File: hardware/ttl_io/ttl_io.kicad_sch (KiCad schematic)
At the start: 26 parts, among them J13 Conn_02x08_Counter_Clockwise, J14 Conn_02x08_Counter_Clockwise, SW3 SW_SPDT, U14 74CBTLV3245, U16 74CBTLV3245, U17 74CBTLV3245, U19 TXB0108

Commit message: update pcb and bom
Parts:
- J13, J14: Link (none) -> https://www.digikey.com/en/products/detail/w%C3%BCrth-elekt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; Manufacturer (none) -> Würth Elektronik; Manufacturer Number (none) -> 610116249121
- SW3: Notes 6V max -> 6V max, may not be washable.
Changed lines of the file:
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@@
       (effects (font (size 1.27 1.27)) hide)
     )
-    (property "Datasheet" "~" (at 86.36 40.005 0)
+    (property "Datasheet" "https://www.we-online.com/components/products/datasheet/6101xx249121.pdf" (at 86.36 40.005 0)
+      (effects (font (size 1.27 1.27)) hide)
+    )
+    (property "Link" "https://www.digikey.com/en/products/detail/w%C3%BCrth-elektronik/610116249121/5047737" (at 86.36 40.005 0)
+      (effects (font (size 1.27 1.27)) hide)
+    )
+    (property "Manufacturer" "Würth Elektronik" (at 86.36 40.005 0)
+      (effects (font (size 1.27 1.27)) hide)
+    )
+    (property "Manufacturer Number" "610116249121" (at 86.36 40.005 0)
       (effects (font (size 1.27 1.27)) hide)
     )
@@
   (symbol (lib_id "Logic_LevelTranslator:TXB0108DQSR") (at 119.38 42.545 180) (unit 1)
     (in_bom yes) (on_board yes) (dnp no)
-    (property "Reference" "U19" (at 125.095 25.4 0)
-      (effects (font (size 1.27 1.27)) (justify left))
-    )
-    (property "Value" "TXB0108" (at 134.62 22.86 0)
-      (effects (font (size 1.27 1.27)) (justify left))
+    (property "Reference" "U19" (at 121.92 23.495 0)
+      (effects (font (size 1.27 1.27)) (justify right))
+    )
+    (property "Value" "TXB0108" (at 121.92 26.035 0)
+      (effects (font (size 1.27 1.27)) (justify right))
     )
     (property "Footprint" "Package_SO:TSSOP-20_4.4x6.5mm_P0.65mm" (at 119.38 23.495 0)
@@
       (effects (font (size 1.27 1.27)) hide)
     )
-    (property "Notes" "6V max" (at 87.63 61.595 90)
+    (property "Notes" "6V max, may not be washable." (at 87.63 61.595 90)
       (effects (font (size 1.27 1.27)) hide)
     )
@@
       (effects (font (size 1.27 1.27)) hide)
     )
-    (property "Datasheet" "~" (at 90.805 166.37 0)
-      (effects (font (size 1.27 1.27)) hide)
-    )
+    (property "Datasheet" "https://www.we-online.com/components/products/datasheet/6101xx249121.pdf" (at 90.805 166.37 0)
+      (effects (font (size 1.27 1.27)) hide)
+    )
+    (property "Link" "https://www.digikey.com/en/products/detail/w%C3%BCrth-elektronik/610116249121/5047737" (at 90.805 166.37 0)
+      (effects (font (size 1.27 1.27)) hide)
+    )
+    (property "Manufacturer" "Würth Elektronik" (at 90.805 166.37 0)
+      (effects (font (size 1.27 1.27)) hide)
+    )
+    (property "Manufacturer Number" "610116249121" (at 90.805 166.37 0)
+      (effects (font (size 1.27 1.27)) hide)
+    )

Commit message: draft scheduler
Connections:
- net EXT_DIR0: now also J13.9 (Pin_9); no longer J13.16 (Pin_16)
- net EXT_DIR1: now also J13.10 (Pin_10); no longer J13.15 (Pin_15)
- net EXT_DIR2: now also J13.11 (Pin_11); no longer J13.14 (Pin_14)
- net EXT_DIR3: now also J13.12 (Pin_12); no longer J13.13 (Pin_13)
- net EXT_DIR4: now also J13.13 (Pin_13); no longer J13.12 (Pin_12)
- net EXT_DIR5: now also J13.14 (Pin_14); no longer J13.11 (Pin_11)
- net EXT_DIR6: now also J13.15 (Pin_15); no longer J13.10 (Pin_10)
- net EXT_DIR7: now also J13.16 (Pin_16); no longer J13.9 (Pin_9)
- net EXT_IN0: now also J14.9 (Pin_9); no longer J14.16 (Pin_16)
- net EXT_IN1: now also J14.10 (Pin_10); no longer J14.15 (Pin_15)
- net EXT_IN2: now also J14.11 (Pin_11); no longer J14.14 (Pin_14)
- net EXT_IN3: now also J14.12 (Pin_12); no longer J14.13 (Pin_13)
- net EXT_IN4: now also J14.13 (Pin_13); no longer J14.12 (Pin_12)
- net EXT_IN5: now also J14.14 (Pin_14); no longer J14.11 (Pin_11)
- net EXT_IN6: now also J14.15 (Pin_15); no longer J14.10 (Pin_10)
- net EXT_IN7: now also J14.16 (Pin_16); no longer J14.9 (Pin_9)
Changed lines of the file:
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@@
     )
   )
-  (symbol (lib_id "Connector_Generic:Conn_02x08_Counter_Clockwise") (at 86.36 40.005 0) (unit 1)
+  (symbol (lib_id "Connector_Generic:Conn_02x08_Counter_Clockwise") (at 86.36 42.545 0) (mirror x) (unit 1)
     (in_bom yes) (on_board yes) (dnp no)
     (property "Reference" "J14" (at 87.63 29.845 0)
       (effects (font (size 1.27 1.27)))
     )
-    (property "Value" "Conn_02x08_Counter_Clockwise" (at 87.63 28.575 0)
-      (effects (font (size 1.27 1.27)) hide)
-    )
-    (property "Footprint" "kicad_component_library:PinHeader_2x08_P2.54mm_Horizontal_SMD" (at 86.36 40.005 0)
-      (effects (font (size 1.27 1.27)) hide)
-    )
-    (property "Datasheet" "https://www.we-online.com/components/products/datasheet/6101xx249121.pdf" (at 86.36 40.005 0)
-      (effects (font (size 1.27 1.27)) hide)
-    )
-    (property "Link" "https://www.digikey.com/en/products/detail/w%C3%BCrth-elektronik/610116249121/5047737" (at 86.36 40.005 0)
-      (effects (font (size 1.27 1.27)) hide)
-    )
-    (property "Manufacturer" "Würth Elektronik" (at 86.36 40.005 0)
-      (effects (font (size 1.27 1.27)) hide)
-    )
-    (property "Manufacturer Number" "610116249121" (at 86.36 40.005 0)
+    (property "Value" "Conn_02x08_Counter_Clockwise" (at 87.63 53.975 0)
+      (effects (font (size 1.27 1.27)) hide)
+    )
+    (property "Footprint" "kicad_component_library:PinHeader_2x08_P2.54mm_Horizontal_SMD" (at 86.36 42.545 0)
+      (effects (font (size 1.27 1.27)) hide)
+    )
+    (property "Datasheet" "https://www.we-online.com/components/products/datasheet/610116249121.pdf" (at 86.36 42.545 0)
+      (effects (font (size 1.27 1.27)) hide)
+    )
+    (property "Link" "https://www.digikey.com/en/products/detail/w%C3%BCrth-elektronik/610116249121/5047737" (at 86.36 42.545 0)
+      (effects (font (size 1.27 1.27)) hide)
+    )
+    (property "Manufacturer" "Würth Elektronik" (at 86.36 42.545 0)
+      (effects (font (size 1.27 1.27)) hide)
+    )
+    (property "Manufacturer Number" "610116249121" (at 86.36 42.545 0)
       (effects (font (size 1.27 1.27)) hide)
     )
@@
     )
   )
-  (symbol (lib_id "Connector_Generic:Conn_02x08_Counter_Clockwise") (at 90.805 166.37 0) (unit 1)
+  (symbol (lib_id "Connector_Generic:Conn_02x08_Counter_Clockwise") (at 90.805 168.91 0) (mirror x) (unit 1)
     (in_bom yes) (on_board yes) (dnp no)
     (property "Reference" "J13" (at 92.075 156.21 0)
       (effects (font (size 1.27 1.27)))
     )
-    (property "Value" "Conn_02x08_Counter_Clockwise" (at 92.075 154.94 0)
-      (effects (font (size 1.27 1.27)) hide)
-    )
-    (property "Footprint" "kicad_component_library:PinHeader_2x08_P2.54mm_Horizontal_SMD" (at 90.805 166.37 0)
-      (effects (font (size 1.27 1.27)) hide)
-    )
-    (property "Datasheet" "https://www.we-online.com/components/products/datasheet/6101xx249121.pdf" (at 90.805 166.37 0)
-      (effects (font (size 1.27 1.27)) hide)
-    )
-    (property "Link" "https://www.digikey.com/en/products/detail/w%C3%BCrth-elektronik/610116249121/5047737" (at 90.805 166.37 0)
-      (effects (font (size 1.27 1.27)) hide)
-    )
-    (property "Manufacturer" "Würth Elektronik" (at 90.805 166.37 0)
-      (effects (font (size 1.27 1.27)) hide)
-    )
-    (property "Manufacturer Number" "610116249121" (at 90.805 166.37 0)
-      (effects (font (size 1.27 1.27)) hide)
-    )
+    (property "Value" "Conn_02x08_Counter_Clockwise" (at 92.075 180.34 0)
+      (effects (font (size 1.27 1.27)) hide)
+    )
+    (property "Footprint" "kicad_component_library:PinHeader_2x08_P2.54mm_Horizontal_SMD" (at 90.805 168.91 0)
+      (effects (font (size 1.27 1.27)) hide)
+    )
+    (property "Datasheet" "https://www.we-online.com/components/products/datasheet/610116249121.pdf" (at 90.805 168.91 0)
+      (effects (font (size 1.27 1.27)) hide)
+    )
+    (property "Link" "https://www.digikey.com/en/products/detail/w%C3%BCrth-elektronik/610116249121/5047737" (at 90.805 168.91 0)
+      (effects (font (size 1.27 1.27)) hide)
+    )
+    (property "Manufacturer" "Würth Elektronik" (at 90.805 168.91 0)
+      (effects (font (size 1.27 1.27)) hide)
+    )
+    (property "Manufacturer Number" "610116249121" (at 90.805 168.91 0)
+      (effects (font (size 1.27 1.27)) hide)
+    )

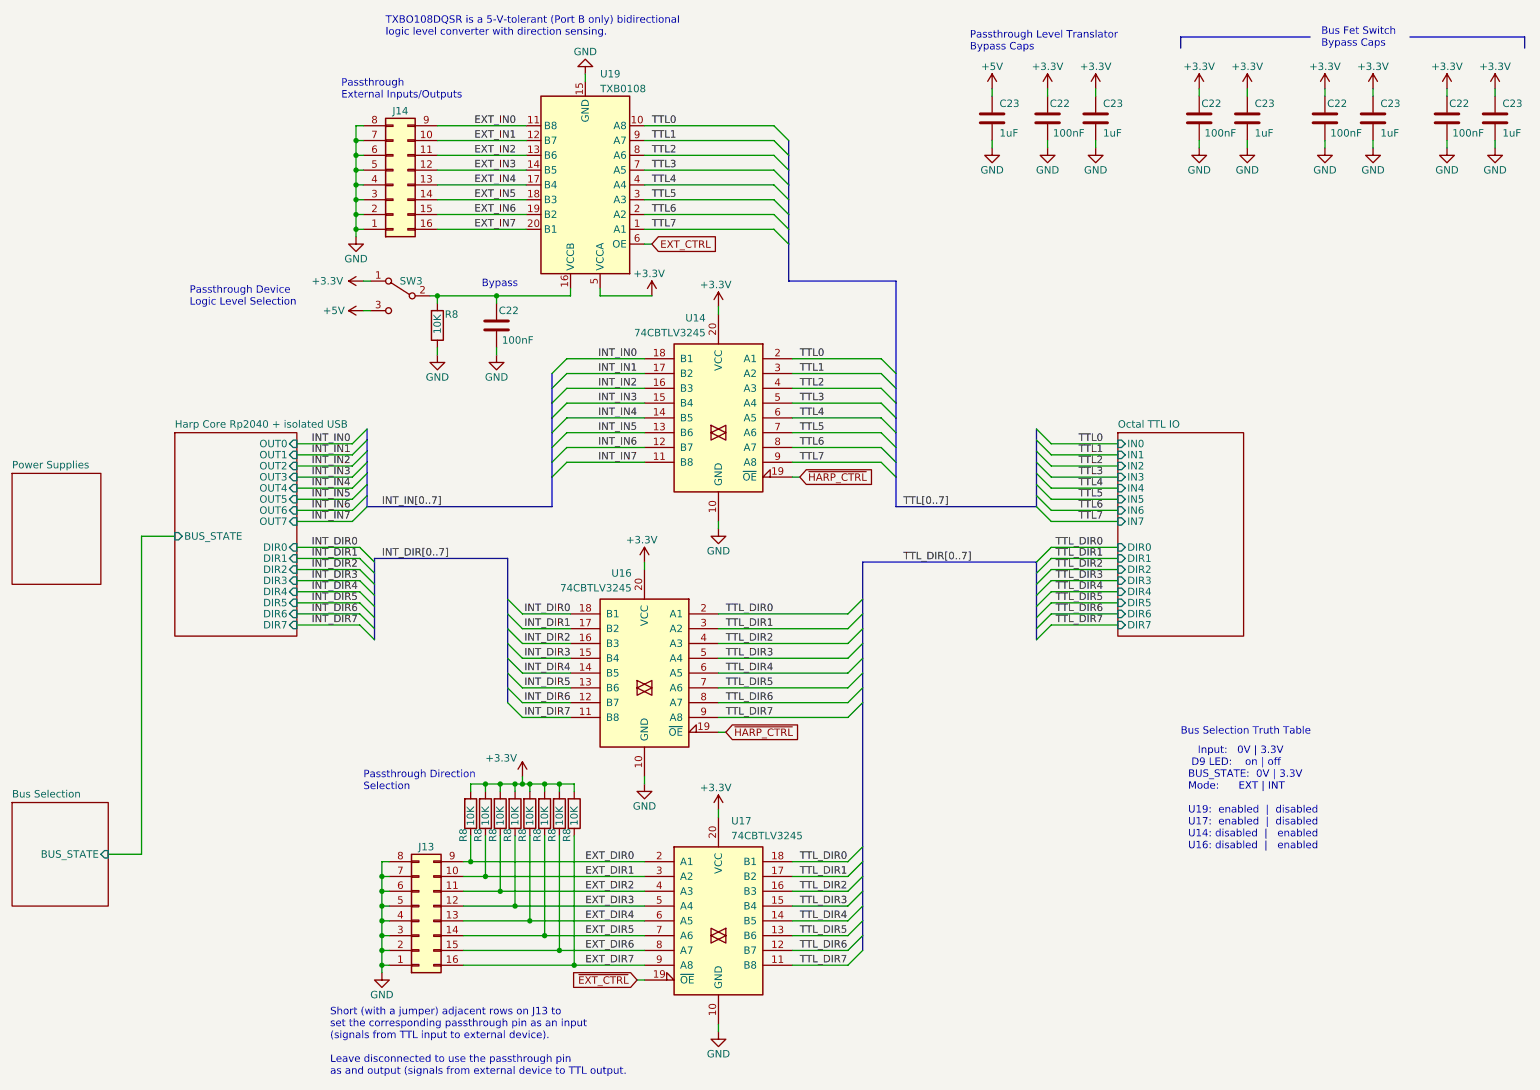
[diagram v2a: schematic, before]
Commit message: get pwm task and ios working
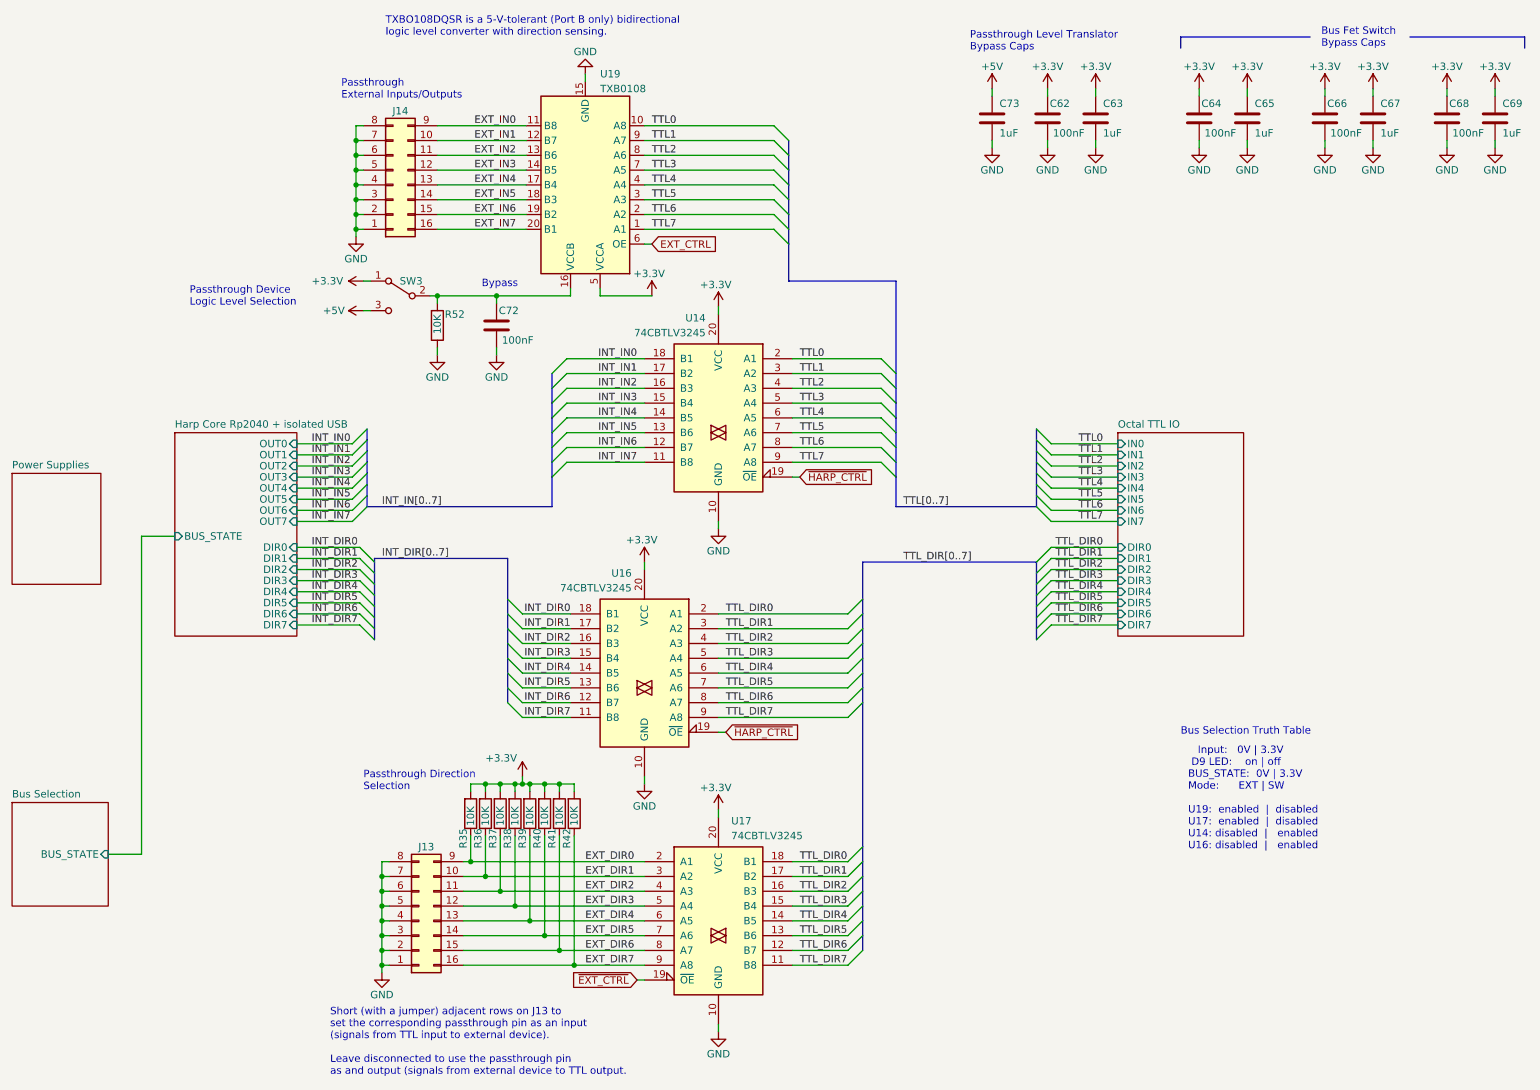
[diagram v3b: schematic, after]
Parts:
- renumbered C22 to C62, C23 to C63, C22 to C64, C23 to C65, C22 to C66, C23 to C67, C22 to C68, C23 to C69, C22 to C72, C23 to C73, R8 to R35, R8 to R36, R8 to R37, R8 to R38, R8 to R39, R8 to R40, R8 to R41, R8 to R42, R8 to R52
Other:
- note added: "Input: 0V | 3.3V D9 LED: on | off BUS_STATE: 0V | 3.3V Mode: EXT | SW U19: enabled | disabled U17: enabled | disabled U14: disabled | enabled U16: disabled | enabled"
- note removed: "Input: 0V | 3.3V D9 LED: on | off BUS_STATE: 0V | 3.3V Mode: EXT | INT U19: enabled | disabled U17: enabled | disabled U14: disabled | enabled U16: disabled | enabled"
